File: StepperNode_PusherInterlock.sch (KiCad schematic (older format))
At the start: 0 parts

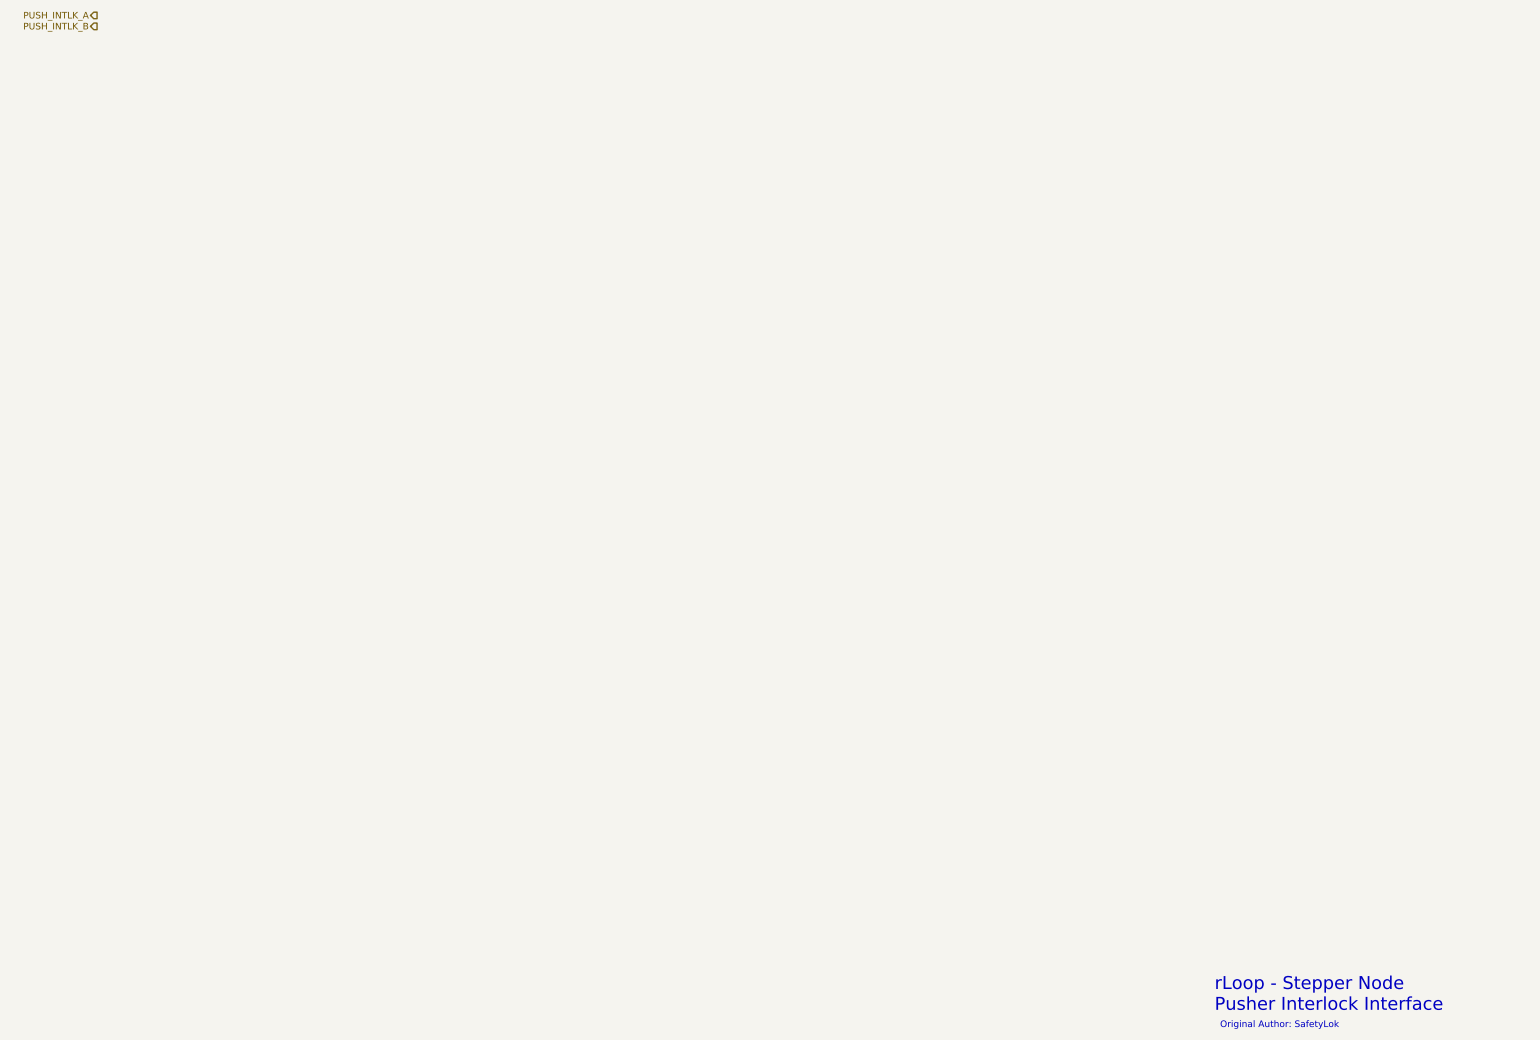
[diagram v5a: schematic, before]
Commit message: Updated node core connector pages and added interlocks.
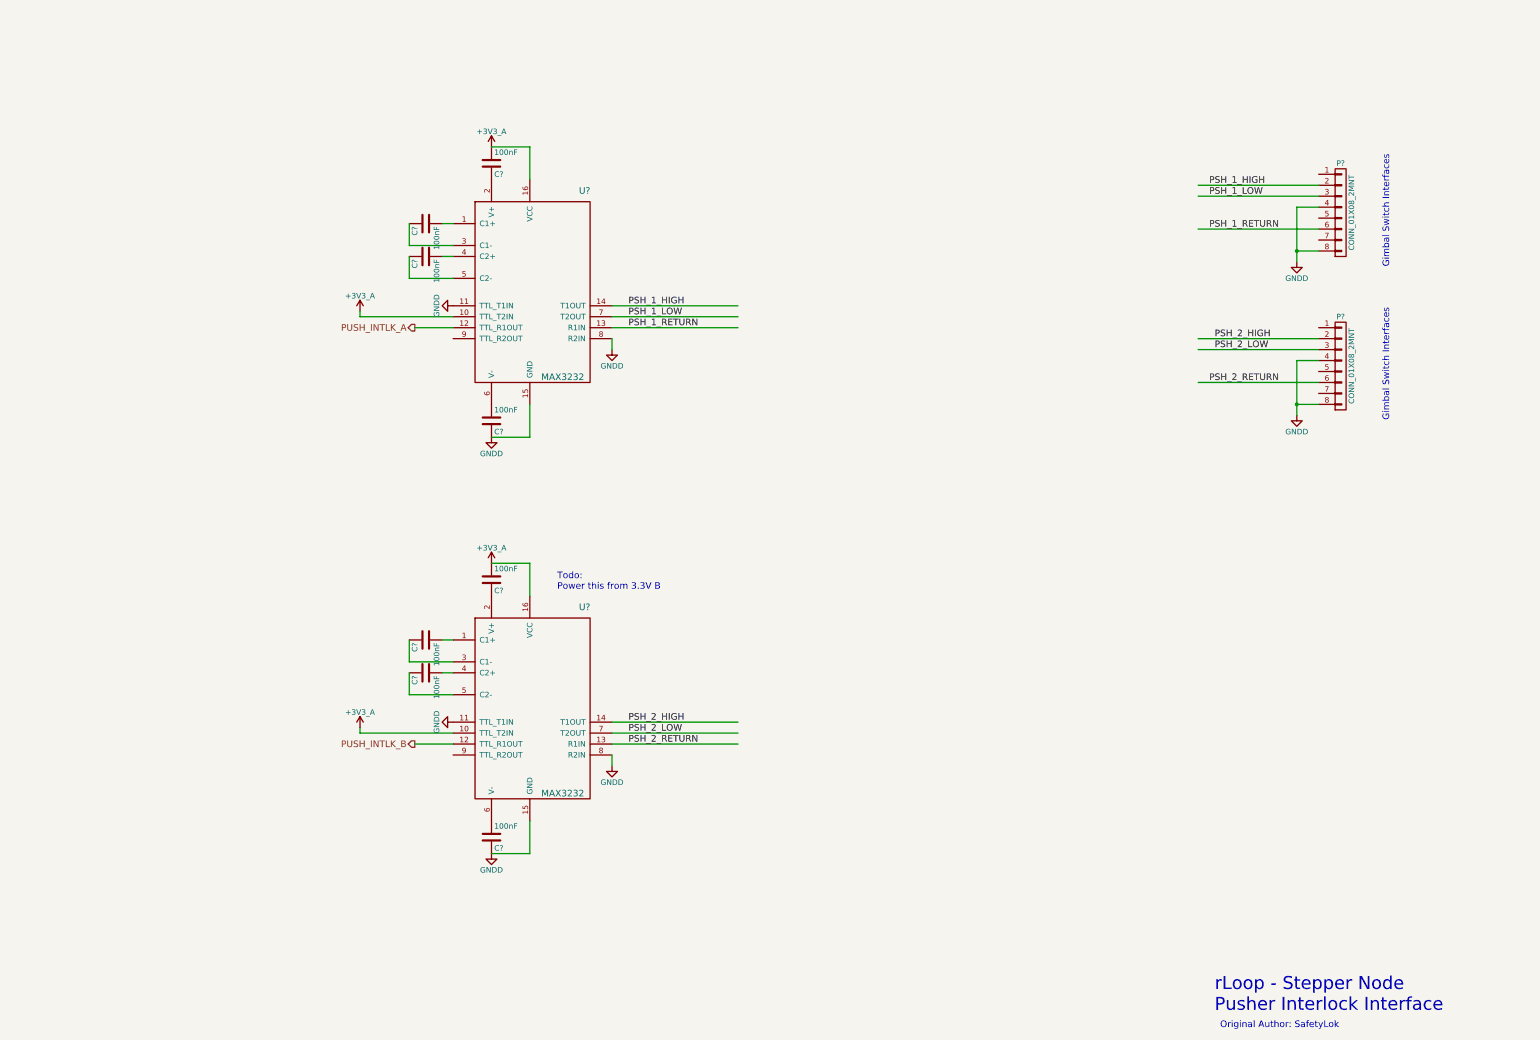
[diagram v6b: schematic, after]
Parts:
- added C? (x8): 100nF, symbol C
- added P? (x2): CONN_01X08_2MNT, symbol CONN_01X08_2MNT
- added U? (x2): MAX3232, symbol MAX3232
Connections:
- net labels added: +3V3_A, GNDD, PSH_1_HIGH, PSH_1_LOW, PSH_1_RETURN, PSH_2_HIGH, PSH_2_LOW, PSH_2_RETURN
- wire segments 0 -> 46
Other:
- note added: "Gimbal Switch Interfaces"
- note added: "Todo:\nPower this from 3.3V B"

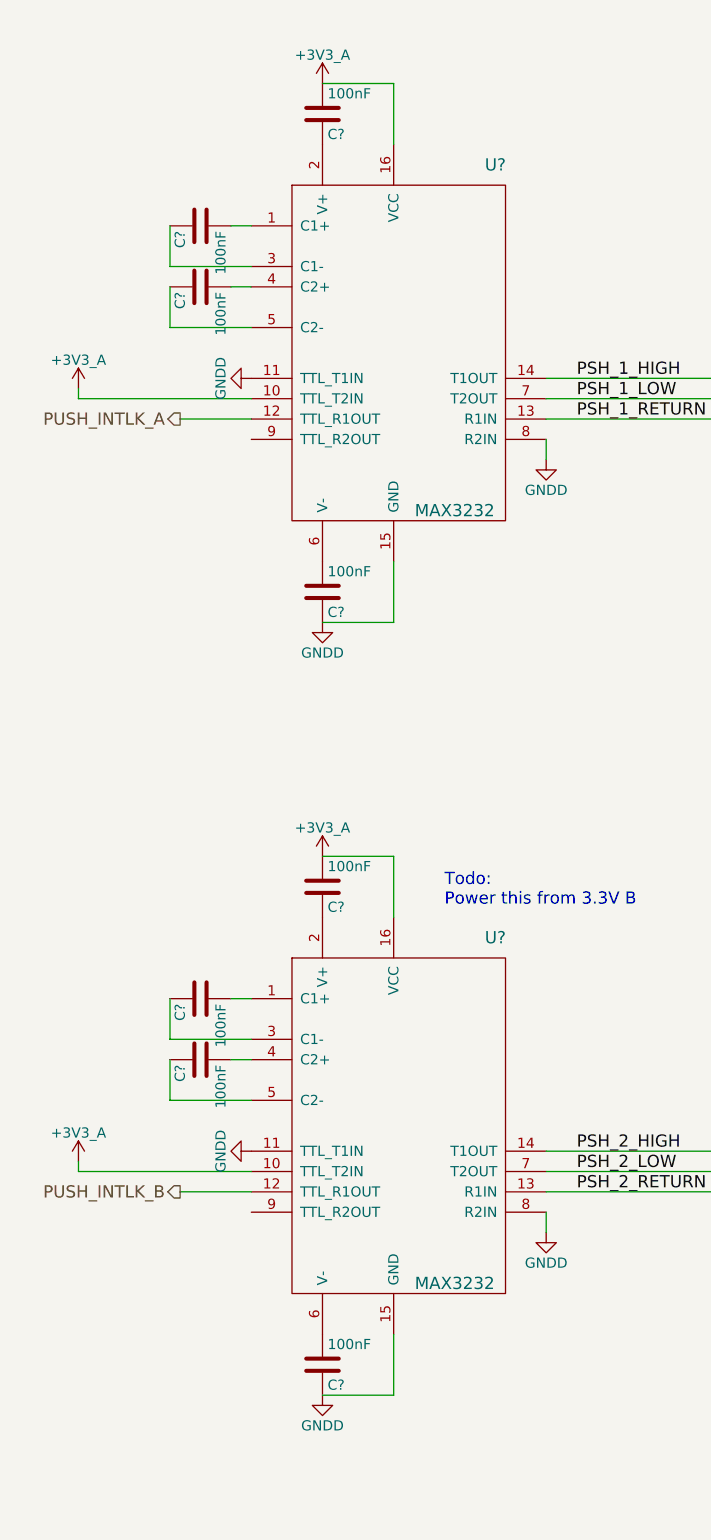
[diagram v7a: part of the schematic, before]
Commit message: Update DAC's and routed gimbal position to MCU direct.
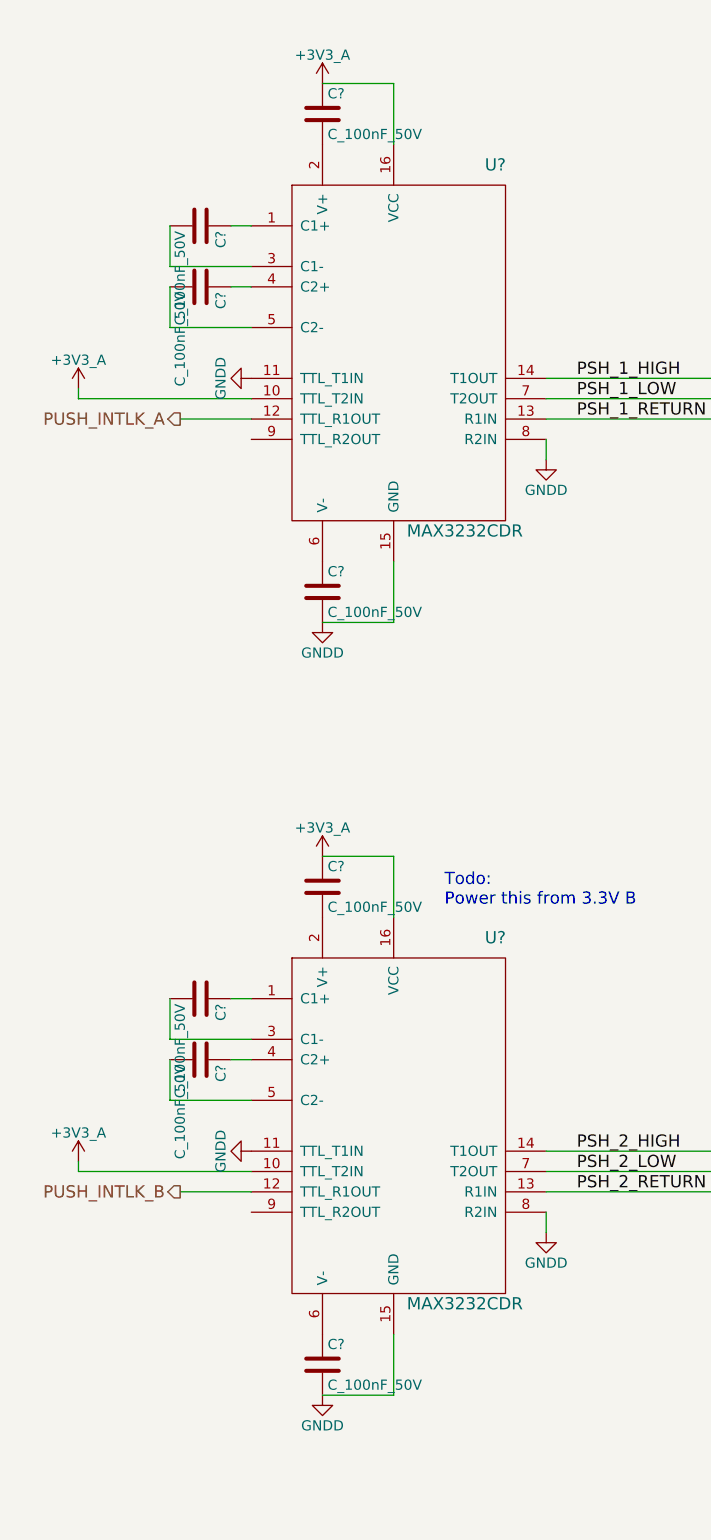
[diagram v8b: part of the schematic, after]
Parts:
- removed C? (x8): 100nF, symbol C
- removed U? (x2): MAX3232, symbol MAX3232
- added C? (x8): C_100nF_50V, RLOOP_FOOTPRINTS:rLoop_C_0603, symbol C_100nF_50V
- added U? (x2): MAX3232CDR, RLOOP_FOOTPRINTS:rLoop_SOIC_16, symbol MAX3232CDR
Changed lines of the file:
@@
 $Descr A3 16535 11693
 encoding utf-8
-Sheet 10 15
+Sheet 5 15
 Title "Pusher Interface Interlock"
 Date ""
@@
 	11750 4600 12850 4600
 $Comp
-L MAX3232 U?
-U 1 1 575DC4AD
-P 5150 2950
-F 0 "U?" H 6150 3050 60  0000 C CNN
-F 1 "MAX3232" H 5950 1350 60  0000 C CNN
-F 2 "" H 5350 2350 60  0000 C CNN
-F 3 "" H 5350 2350 60  0000 C CNN
-	1    5150 2950
-	1    0    0    -1
-$EndComp
-$Comp
-L C C?
-U 1 1 575DC4B4
-P 4700 3150
-F 0 "C?" H 4725 3250 50  0000 L CNN
-F 1 "100nF" H 4725 3050 50  0000 L CNN
-F 2 "" H 4738 3000 50  0000 C CNN
-F 3 "" H 4700 3150 50  0000 C CNN
-	1    4700 3150
-	0    -1   1    0
-$EndComp
-$Comp
-L C C?
-U 1 1 575DC4BB
-P 4700 3450
-F 0 "C?" H 4725 3550 50  0000 L CNN
-F 1 "100nF" H 4725 3350 50  0000 L CNN
-F 2 "" H 4738 3300 50  0000 C CNN
-F 3 "" H 4700 3450 50  0000 C CNN
-	1    4700 3450
-	0    -1   1    0
-$EndComp
-$Comp
-L C C?
-U 1 1 575DC4C2
-P 5300 2600
-F 0 "C?" H 5325 2700 50  0000 L CNN
-F 1 "100nF" H 5325 2500 50  0000 L CNN
-F 2 "" H 5338 2450 50  0000 C CNN
-F 3 "" H 5300 2600 50  0000 C CNN
-	1    5300 2600
-	1    0    0    1
-$EndComp
-$Comp
-L C C?
-U 1 1 575DC4C9
-P 5300 4950
-F 0 "C?" H 5325 5050 50  0000 L CNN
-F 1 "100nF" H 5325 4850 50  0000 L CNN
-F 2 "" H 5338 4800 50  0000 C CNN
-F 3 "" H 5300 4950 50  0000 C CNN
-	1    5300 4950
-	1    0    0    1
-$EndComp
-$Comp
 L GNDD #PWR?
 U 1 1 575DC4D0
@@
 Text HLabel 4600 7900 0    60   Output ~ 0
 PUSH_INTLK_B
-$Comp
-L MAX3232 U?
-U 1 1 575DCEF2
-P 5150 6750
-F 0 "U?" H 6150 6850 60  0000 C CNN
-F 1 "MAX3232" H 5950 5150 60  0000 C CNN
-F 2 "" H 5350 6150 60  0000 C CNN
-F 3 "" H 5350 6150 60  0000 C CNN
-	1    5150 6750
-	1    0    0    -1
-$EndComp
-$Comp
-L C C?
-U 1 1 575DCEF8
-P 4700 6950
-F 0 "C?" H 4725 7050 50  0000 L CNN
-F 1 "100nF" H 4725 6850 50  0000 L CNN
-F 2 "" H 4738 6800 50  0000 C CNN
-F 3 "" H 4700 6950 50  0000 C CNN
-	1    4700 6950
-	0    -1   1    0
-$EndComp
-$Comp
-L C C?
-U 1 1 575DCEFE
-P 4700 7250
-F 0 "C?" H 4725 7350 50  0000 L CNN
-F 1 "100nF" H 4725 7150 50  0000 L CNN
-F 2 "" H 4738 7100 50  0000 C CNN
-F 3 "" H 4700 7250 50  0000 C CNN
-	1    4700 7250
-	0    -1   1    0
-$EndComp
-$Comp
-L C C?
-U 1 1 575DCF04
-P 5300 6400
-F 0 "C?" H 5325 6500 50  0000 L CNN
-F 1 "100nF" H 5325 6300 50  0000 L CNN
-F 2 "" H 5338 6250 50  0000 C CNN
-F 3 "" H 5300 6400 50  0000 C CNN
-	1    5300 6400
-	1    0    0    1
-$EndComp
-$Comp
-L C C?
-U 1 1 575DCF0A
-P 5300 8750
-F 0 "C?" H 5325 8850 50  0000 L CNN
-F 1 "100nF" H 5325 8650 50  0000 L CNN
-F 2 "" H 5338 8600 50  0000 C CNN
-F 3 "" H 5300 8750 50  0000 C CNN
-	1    5300 8750
-	1    0    0    1
-$EndComp
 $Comp
 L GNDD #PWR?
@@
 Text Label 11850 4600 0    60   ~ 0
 PSH_2_RETURN
+$Comp
+L MAX3232CDR U?
+U 1 1 575A130F
+P 5150 2950
+F 0 "U?" H 6150 3050 60  0000 C CNN
+F 1 "MAX3232CDR" H 6000 1250 60  0000 C CNN
+F 2 "RLOOP_FOOTPRINTS:rLoop_SOIC_16" H 5350 2350 60  0001 C CNN
+F 3 "" H 5350 2350 60  0000 C CNN
+	1    5150 2950
+	1    0    0    -1
+$EndComp
+$Comp
+L MAX3232CDR U?
+U 1 1 575A140C
+P 5150 6750
+F 0 "U?" H 6150 6850 60  0000 C CNN
+F 1 "MAX3232CDR" H 6000 5050 60  0000 C CNN
+F 2 "RLOOP_FOOTPRINTS:rLoop_SOIC_16" H 5350 6150 60  0001 C CNN
+F 3 "" H 5350 6150 60  0000 C CNN
+	1    5150 6750
+	1    0    0    -1
+$EndComp
+$Comp
+L C_100nF_50V C?
+U 1 1 575A15C1
+P 5300 6400
+F 0 "C?" H 5325 6500 50  0000 L CNN
+F 1 "C_100nF_50V" H 5325 6300 50  0000 L CNN
+F 2 "RLOOP_FOOTPRINTS:rLoop_C_0603" H 5338 6250 50  0001 C CNN
+F 3 "" H 5300 6400 50  0000 C CNN
+	1    5300 6400
+	1    0    0    -1
+$EndComp
+$Comp
+L C_100nF_50V C?
+U 1 1 575A1648
+P 4700 6950
+F 0 "C?" H 4725 7050 50  0000 L CNN
+F 1 "C_100nF_50V" H 4725 6850 50  0000 L CNN
+F 2 "RLOOP_FOOTPRINTS:rLoop_C_0603" H 4738 6800 50  0001 C CNN
+F 3 "" H 4700 6950 50  0000 C CNN
+	1    4700 6950
+	0    1    1    0
+$EndComp
+$Comp
+L C_100nF_50V C?
+U 1 1 575A16FF
+P 5300 8750
+F 0 "C?" H 5325 8850 50  0000 L CNN
+F 1 "C_100nF_50V" H 5325 8650 50  0000 L CNN
+F 2 "RLOOP_FOOTPRINTS:rLoop_C_0603" H 5338 8600 50  0001 C CNN
+F 3 "" H 5300 8750 50  0000 C CNN
+	1    5300 8750
+	1    0    0    -1
+$EndComp
+$Comp
+L C_100nF_50V C?
+U 1 1 575A189E
+P 5300 4950
+F 0 "C?" H 5325 5050 50  0000 L CNN
+F 1 "C_100nF_50V" H 5325 4850 50  0000 L CNN
+F 2 "RLOOP_FOOTPRINTS:rLoop_C_0603" H 5338 4800 50  0001 C CNN
+F 3 "" H 5300 4950 50  0000 C CNN
+	1    5300 4950
+	1    0    0    -1
+$EndComp
+$Comp
+L C_100nF_50V C?
+U 1 1 575A1A4C
+P 5300 2600
+F 0 "C?" H 5325 2700 50  0000 L CNN
+F 1 "C_100nF_50V" H 5325 2500 50  0000 L CNN
+F 2 "RLOOP_FOOTPRINTS:rLoop_C_0603" H 5338 2450 50  0001 C CNN
+F 3 "" H 5300 2600 50  0000 C CNN
+	1    5300 2600
+	1    0    0    -1
+$EndComp
+$Comp
+L C_100nF_50V C?
+U 1 1 575A1C14
+P 4700 7250
+F 0 "C?" H 4725 7350 50  0000 L CNN
+F 1 "C_100nF_50V" H 4725 7150 50  0000 L CNN
+F 2 "RLOOP_FOOTPRINTS:rLoop_C_0603" H 4738 7100 50  0001 C CNN
+F 3 "" H 4700 7250 50  0000 C CNN
+	1    4700 7250
+	0    1    1    0
+$EndComp
+$Comp
+L C_100nF_50V C?
+U 1 1 575A1F38
+P 4700 3150
+F 0 "C?" H 4725 3250 50  0000 L CNN
+F 1 "C_100nF_50V" H 4725 3050 50  0000 L CNN
+F 2 "RLOOP_FOOTPRINTS:rLoop_C_0603" H 4738 3000 50  0001 C CNN
+F 3 "" H 4700 3150 50  0000 C CNN
+	1    4700 3150
+	0    1    1    0
+$EndComp
+$Comp
+L C_100nF_50V C?
+U 1 1 575A1FCB
+P 4700 3450
+F 0 "C?" H 4725 3550 50  0000 L CNN
+F 1 "C_100nF_50V" H 4725 3350 50  0000 L CNN
+F 2 "RLOOP_FOOTPRINTS:rLoop_C_0603" H 4738 3300 50  0001 C CNN
+F 3 "" H 4700 3450 50  0000 C CNN
+	1    4700 3450
+	0    1    1    0
+$EndComp
 $EndSCHEMATC
